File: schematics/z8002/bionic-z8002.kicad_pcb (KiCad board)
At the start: 2 copper layers, 25.4 x 68.6 mm, 8 parts, among them J1 Bionic-P135, J2 Bionic-P245, U1 Z8002, U2 11AA010-I/TT

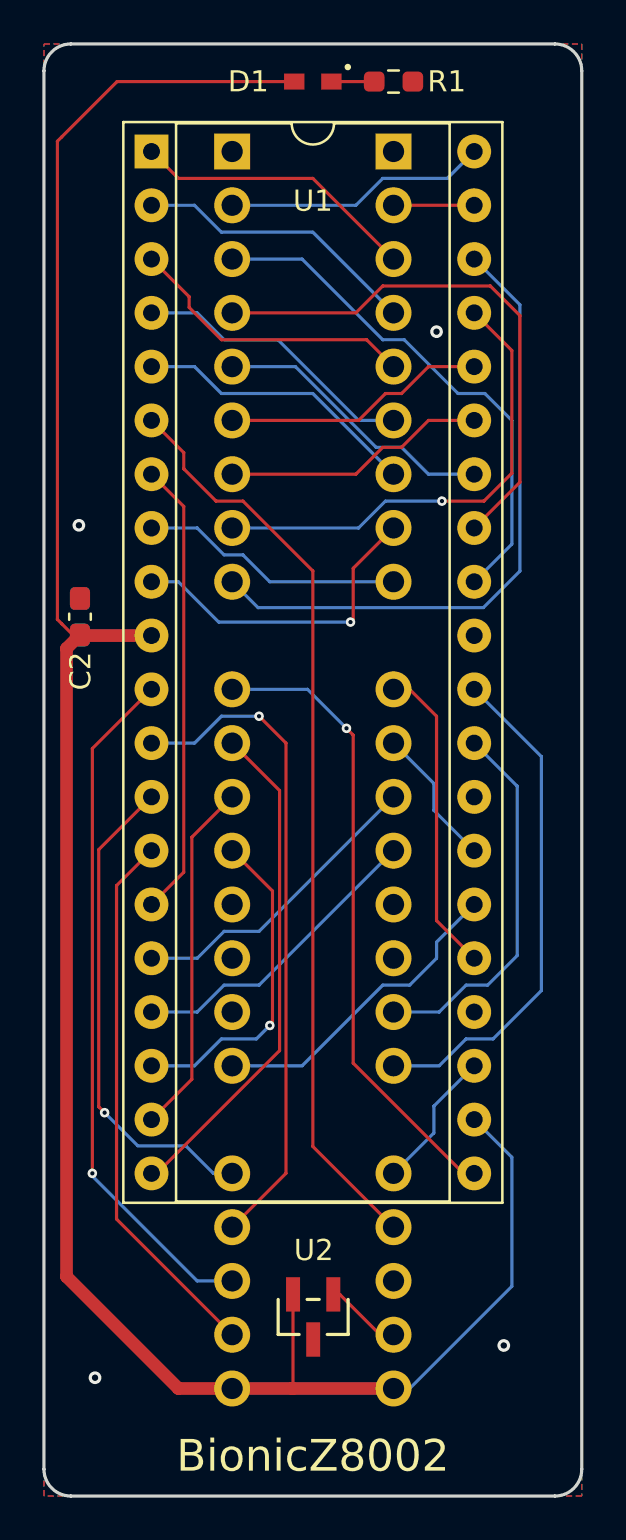
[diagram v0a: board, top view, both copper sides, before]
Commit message: [schematics] Straighten board tracks and regenerate Gerbers
straighten_tracks.py on every routed board: router leftovers snapped to
0/45/90 degrees and redundant segments merged, each pass DRC-checked
(counts unchanged). Gerbers and drill files of the changed boards are
regenerated with each board's plot settings, keeping the committed file
sets; tms9980 keeps its tracks (the rebuild left a dangling VCC stub).
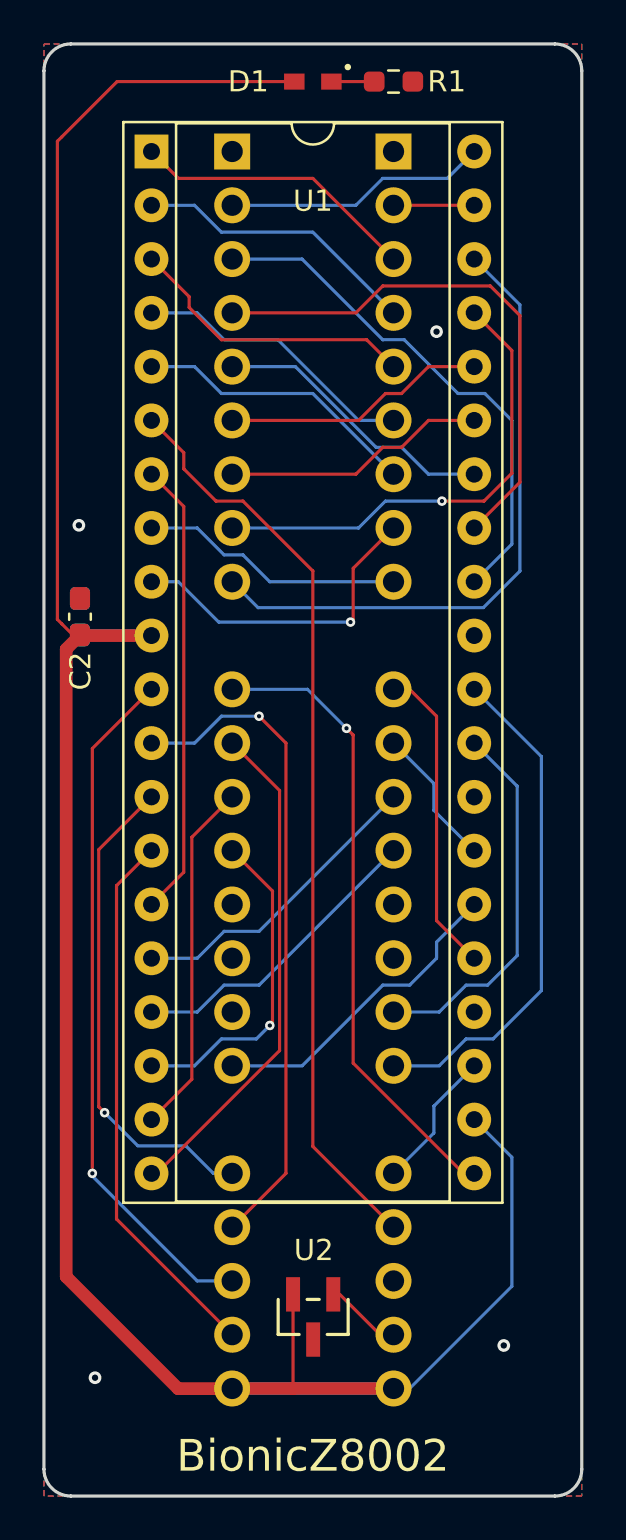
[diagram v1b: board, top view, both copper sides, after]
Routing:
- net VCC: track 119.6 -> 118.0 mm
- net Net-(J2-P57): track 3.63 -> 2.69 mm
- net R/~{W}: track 14.7 -> 14.0 mm
- net ST0: track 30.0 -> 29.5 mm
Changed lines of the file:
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@@
+	)
+	(gr_arc
+		(start 101 71.27)
+		(mid 101.371974 70.371974)
+		(end 102.27 70)
+		(stroke
+			(width 0.15)
+			(type default)
+		)
+		(layer "Edge.Cuts")
+	)
+	(gr_line
+		(start 101 137.31)
+		(end 101 71.27)
+		(stroke
+			(width 0.15)
+			(type default)
+		)
+		(layer "Edge.Cuts")
+	)
+	(gr_line
+		(start 102.27 70)
+		(end 125.13 70)
+		(stroke
+			(width 0.15)
+			(type default)
+		)
+		(layer "Edge.Cuts")
+	)
+	(gr_arc
+		(start 102.27 138.58)
+		(mid 101.371974 138.208026)
+		(end 101 137.31)
+		(stroke
+			(width 0.15)
+			(type default)
+		)
+		(layer "Edge.Cuts")
 	)
 	(gr_arc
@@
 		(layer "Edge.Cuts")
 	)
-	(gr_arc
-		(start 126.4 137.31)
-		(mid 126.028026 138.208026)
-		(end 125.13 138.58)
-		(stroke
-			(width 0.15)
-			(type default)
-		)
-		(layer "Edge.Cuts")
-	)
-	(gr_arc
-		(start 101 71.27)
-		(mid 101.371974 70.371974)
-		(end 102.27 70)
+	(gr_line
+		(start 125.13 138.58)
+		(end 102.27 138.58)
 		(stroke
 			(width 0.15)
@@
 	)
 	(gr_arc
-		(start 102.27 138.58)
-		(mid 101.371974 138.208026)
-		(end 101 137.31)
-		(stroke
-			(width 0.15)
-			(type default)
-		)
-		(layer "Edge.Cuts")
-	)
-	(gr_line
-		(start 125.13 138.58)
-		(end 102.27 138.58)
-		(stroke
-			(width 0.15)
-			(type default)
-		)
-		(layer "Edge.Cuts")
-	)
-	(gr_line
-		(start 101 137.31)
-		(end 101 71.27)
-		(stroke
-			(width 0.15)
-			(type default)
-		)
-		(layer "Edge.Cuts")
-	)
-	(gr_line
-		(start 102.27 70)
-		(end 125.13 70)
+		(start 126.4 137.31)
+		(mid 126.028026 138.208026)
+		(end 125.13 138.58)
 		(stroke
 			(width 0.15)
@@
 		)
 	)
+	(gr_text "JLCJLCJLCJLC"
+		(at 113.7 137.564 -0)
+		(layer "B.SilkS")
+		(effects
+			(font
+				(size 0.8 0.8)
+				(thickness 0.1)
+			)
+			(justify bottom mirror)
+		)
+	)
 	(gr_text "Rev. 1"
 		(at 107.096 137.564 -0)
@@
 		)
 	)
-	(gr_text "JLCJLCJLCJLC"
-		(at 113.7 137.564 -0)
-		(layer "B.SilkS")
-		(effects
-			(font
-				(size 0.8 0.8)
-				(thickness 0.1)
-			)
-			(justify bottom mirror)
-		)
-	)
 	(via
 		(at 102.651 92.733)
@@
 	)
 	(segment
-		(start 109.9108 133.5)
-		(end 109.89 133.5)
-		(width 0.6)
-		(layer "F.Cu")
-		(net 2)
-	)
-	(segment
-		(start 112.735 133.5)
-		(end 109.89 133.5)
+		(start 109.89 133.5)
+		(end 112.7652 133.5)
 		(width 0.6)
 		(locked yes)
@@
 	)
 	(segment
-		(start 107.35 133.5)
-		(end 102.0668 128.2168)
+		(start 112.7652 133.5)
+		(end 112.7652 129.055)
+		(width 0.15)
+		(locked yes)
+		(layer "F.Cu")
+		(net 2)
+	)
+	(segment
+		(start 101.635 97.1782)
+		(end 101.838 97.3812)
+		(width 0.15)
+		(layer "F.Cu")
+		(net 2)
+	)
+	(segment
+		(start 112.824 71.778)
+		(end 104.4541 71.7781)
+		(width 0.15)
+		(locked yes)
+		(layer "F.Cu")
+		(net 2)
+	)
+	(segment
+		(start 117.51 133.5)
+		(end 112.7652 133.5)
 		(width 0.6)
 		(locked yes)
@@
 	)
 	(segment
-		(start 112.7652 129.055)
-		(end 112.765 129.055)
-		(width 0.6)
-		(layer "F.Cu")
-		(net 2)
-	)
-	(segment
-		(start 102.0668 98.5496)
-		(end 102.6764 97.94)
+		(start 107.335589 133.5068)
+		(end 102.052765 128.223976)
 		(width 0.6)
 		(locked yes)
@@
 	)
 	(segment
-		(start 102.7018 97.9146)
-		(end 102.702 97.9146)
-		(width 0.15)
+		(start 102.052765 98.582176)
+		(end 102.7018 97.9332)
+		(width 0.6)
 		(locked yes)
 		(layer "F.Cu")
@@
 	)
 	(segment
-		(start 112.765199 129.055)
-		(end 112.765199 133.469801)
+		(start 104.4541 71.7781)
+		(end 101.838 74.3942)
 		(width 0.15)
 		(locked yes)
@@
 	)
 	(segment
-		(start 101.635 97.1782)
-		(end 101.838 97.3812)
-		(width 0.15)
-		(layer "F.Cu")
-		(net 2)
-	)
-	(segment
-		(start 102.6764 97.94)
+		(start 101.635 74.5972)
+		(end 101.635 97.1782)
+		(width 0.15)
+		(layer "F.Cu")
+		(net 2)
+	)
+	(segment
+		(start 102.7018 97.94)
 		(end 106.08 97.94)
 		(width 0.6)
@@
 	)
 	(segment
-		(start 112.8237 71.778)
-		(end 104.454 71.778)
-		(width 0.15)
-		(locked yes)
-		(layer "F.Cu")
-		(net 2)
-	)
-	(segment
-		(start 117.51 133.5)
-		(end 112.735 133.5)
+		(start 102.052765 128.223976)
+		(end 102.052765 98.582176)
 		(width 0.6)
 		(locked yes)
@@
 	)
 	(segment
-		(start 104.454 71.778)
-		(end 101.838 74.3942)
-		(width 0.15)
-		(locked yes)
-		(layer "F.Cu")
-		(net 2)
-	)
-	(segment
-		(start 109.89 133.5)
-		(end 107.35 133.5)
+		(start 109.89 133.5068)
+		(end 107.335589 133.5068)
 		(width 0.6)
 		(locked yes)
@@
 	)
 	(segment
-		(start 102.372 97.9146)
-		(end 102.7018 97.9146)
-		(width 0.15)
-		(locked yes)
-		(layer "F.Cu")
-		(net 2)
-	)
-	(segment
-		(start 101.635 74.5972)
-		(end 101.635 97.1782)
-		(width 0.15)
-		(layer "F.Cu")
-		(net 2)
-	)
-	(segment
-		(start 102.0668 128.2168)
-		(end 102.0668 98.5496)
-		(width 0.6)
-		(locked yes)
-		(layer "F.Cu")
-		(net 2)
-	)
-	(segment
-		(start 112.765199 133.469801)
-		(end 112.735 133.5)
-		(width 0.15)
-		(locked yes)
-		(layer "F.Cu")
-		(net 2)
-	)
-	(segment
-		(start 112.824 71.778)
-		(end 112.8237 71.778)
-		(width 0.15)
-		(locked yes)
-		(layer "F.Cu")
-		(net 2)
-	)
-	(segment
-		(start 102.7272 97.94)
-		(end 102.7018 97.9146)
-		(width 0.15)
-		(locked yes)
-		(layer "F.Cu")
-		(net 2)
-	)
-	(segment
 		(start 101.838 74.3942)
 		(end 101.635 74.5972)
@@
 	)
 	(segment
-		(start 117.4846 133.5)
-		(end 109.9108 133.5)
-		(width 0.6)
-		(layer "B.Cu")
-		(net 2)
-	)
-	(segment
 		(start 106.08 97.94)
-		(end 103.135 97.94)
-		(width 0.6)
-		(locked yes)
-		(layer "B.Cu")
-		(net 2)
-	)
-	(segment
-		(start 102.7018 97.9146)
-		(end 103.1097 97.9146)
-		(width 0.6)
-		(locked yes)
-		(layer "B.Cu")
-		(net 2)
-	)
-	(segment
-		(start 123.098 128.674)
-		(end 118.272 133.5)
-		(width 0.15)
-		(layer "B.Cu")
-		(net 2)
-	)
-	(segment
-		(start 103.135 97.94)
 		(end 103.134 97.9389)
 		(width 0.6)
@@
 	)
 	(segment
+		(start 123.098 128.674)
+		(end 118.272 133.5)
+		(width 0.15)
+		(layer "B.Cu")
+		(net 2)
+	)
+	(segment
 		(start 121.32 120.8)
 		(end 123.098 122.578)
@@
 	)
 	(segment
-		(start 103.1097 97.9146)
-		(end 103.134 97.9389)
-		(width 0.6)
-		(locked yes)
-		(layer "B.Cu")
-		(net 2)
-	)
-	(segment
-		(start 102.7018 97.9146)
-		(end 102.702 97.9146)
-		(width 0.6)
-		(layer "B.Cu")
-		(net 2)
-	)
-	(segment
 		(start 123.098 122.578)
 		(end 123.098 128.674)
@@
 	)
 	(segment
-		(start 118.272 133.5)
-		(end 117.4846 133.5)
-		(width 0.15)
+		(start 117.51 133.5)
+		(end 109.89 133.5)
+		(width 0.6)
 		(layer "B.Cu")
 		(net 2)
@@
 		(layer "F.Cu")
 		(net 5)
-	)
-	(segment
-		(start 117.51 130.96)
-		(end 116.875 130.96)
-		(width 0.15)
-		(layer "F.Cu")
-		(net 6)
-	)
-	(segment
-		(start 114.97 129.055)
-		(end 114.6652 129.055)
-		(width 0.15)
-		(layer "F.Cu")
-		(net 6)
 	)
 	(segment
@@
 	)
 	(segment
-		(start 120.812 123.34)
-		(end 121.32 123.34)
-		(width 0.15)
-		(layer "F.Cu")
-		(net 16)
-	)
-	(segment
 		(start 115.605 118.133)
 		(end 120.812 123.34)
@@
 	)
 	(segment
-		(start 106.331694 123.34)
-		(end 106.08 123.34)
-		(width 0.15)
-		(layer "F.Cu")
-		(net 21)
-	)
-	(segment
 		(start 112.129 105.259)
 		(end 112.129 117.542694)
@@
 		(width 0.15)
 		(layer "F.Cu")
-		(net 42)
-	)
-	(segment
-		(start 117.51 100.48)
-		(end 118.272 100.48)
-		(width 0.15)
-		(layer "F.Cu")

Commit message: [schematics] Remove the JLC order-number marker from all boards
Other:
- board text removed: "JLCJLCJLCJLC"
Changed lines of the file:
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@@
-		)
-	)
-	(gr_text "JLCJLCJLCJLC"
-		(at 113.7 137.564 -0)
-		(layer "B.SilkS")
-		(effects
-			(font
-				(size 0.8 0.8)
-				(thickness 0.1)
-			)
-			(justify bottom mirror)
 		)
 	)
